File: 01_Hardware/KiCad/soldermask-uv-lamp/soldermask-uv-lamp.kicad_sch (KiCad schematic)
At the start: 12 parts, among them J1 USB_C_Receptacle_USB2.0_16P, Q1 BC817

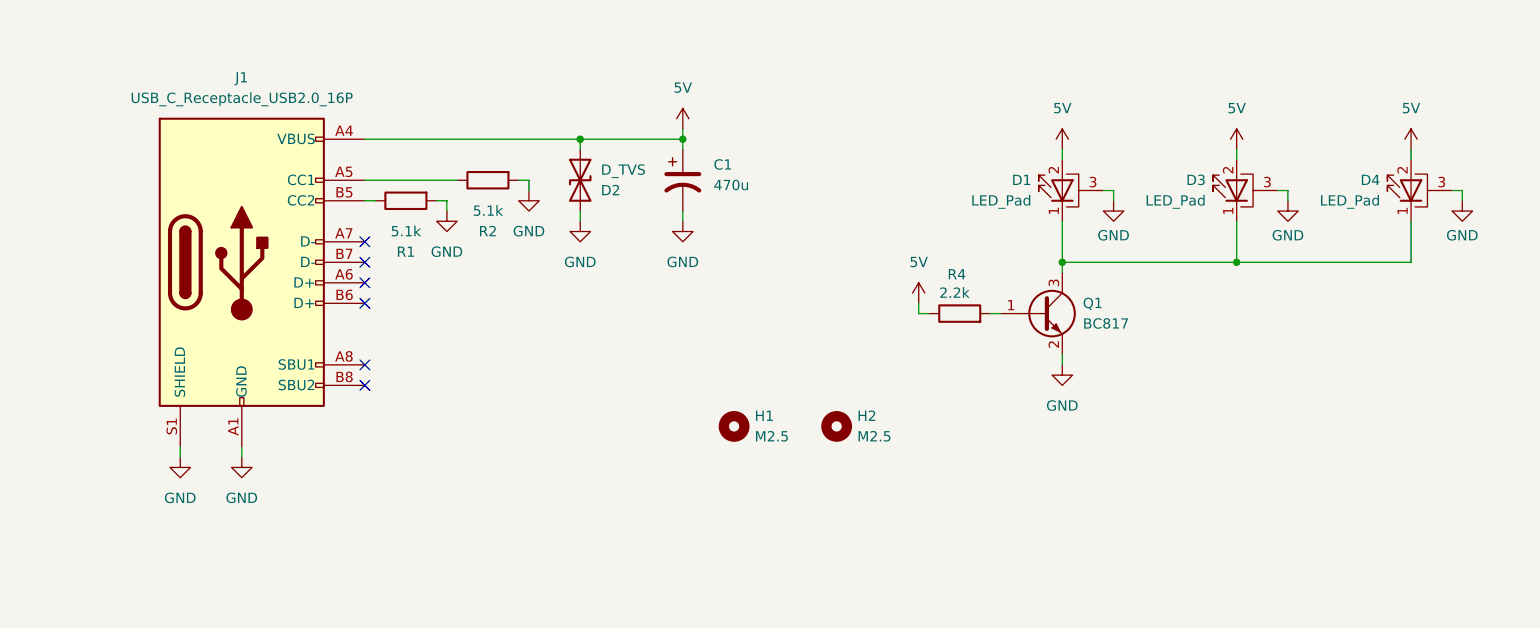
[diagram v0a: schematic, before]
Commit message: Added captions to schematics and pcb design
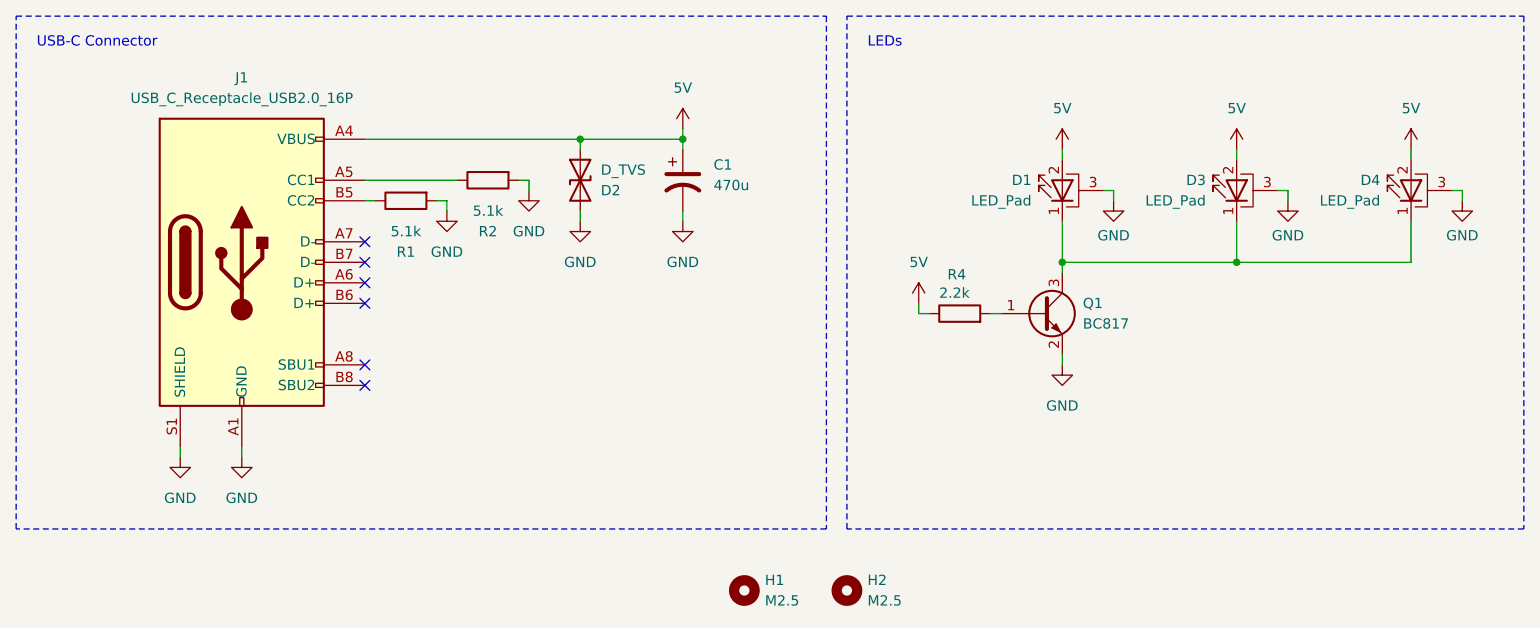
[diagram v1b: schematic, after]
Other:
- note added: "LEDs"
- note added: "USB-C Connector"
- company: (none) -> Szymon Wąchała
- title: (none) -> Soldermask UV Lamp
- moved on the sheet: H1, H2
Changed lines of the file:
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@@
 	(generator_version "9.0")
 	(paper "A4")
+	(title_block
+		(title "Soldermask UV Lamp")
+		(date "2025-11-21")
+		(rev "0.1")
+		(company "Szymon Wąchała")
+	)
+	(rectangle
+		(start 153.67 63.5)
+		(end 237.49 127)
+		(stroke
+			(width 0)
+			(type dash_dot)
+		)
+		(fill
+			(type none)
+		)
+	)
+	(rectangle
+		(start 50.8 63.5)
+		(end 151.13 127)
+		(stroke
+			(width 0)
+			(type dash_dot)
+		)
+		(fill
+			(type none)
+		)
+	)
+	(text "USB-C Connector"
+		(exclude_from_sim no)
+		(at 53.34 66.802 0)
+		(effects
+			(font
+				(size 1.27 1.27)
+			)
+			(justify left)
+		)
+	)
+	(text "LEDs"
+		(exclude_from_sim no)
+		(at 156.21 66.802 0)
+		(effects
+			(font
+				(size 1.27 1.27)
+			)
+			(justify left)
+		)
+	)
 	(junction
 		(at 120.65 78.74)
@@
 	(symbol
 		(lib_id "Mechanical:MountingHole")
-		(at 152.4 114.3 0)
+		(at 153.67 134.62 0)
 		(unit 1)
 		(exclude_from_sim no)
@@
 		(fields_autoplaced yes)
 		(property "Reference" "H2"
-			(at 154.94 113.0299 0)
+			(at 156.21 133.3499 0)
 			(effects
 				(font
@@
 		)
 		(property "Value" "M2.5"
-			(at 154.94 115.5699 0)
+			(at 156.21 135.8899 0)
 			(effects
 				(font
@@
 		)
 		(property "Footprint" "MountingHole:MountingHole_2.7mm_M2.5"
-			(at 152.4 114.3 0)
+			(at 153.67 134.62 0)
 			(effects
 				(font
@@
 		)
 		(property "Datasheet" "~"
-			(at 152.4 114.3 0)
+			(at 153.67 134.62 0)
 			(effects
 				(font
@@
 		)
 		(property "Description" "Mounting Hole without connection"
-			(at 152.4 114.3 0)
+			(at 153.67 134.62 0)
 			(effects
 				(font
@@
 	(symbol
 		(lib_id "Mechanical:MountingHole")
-		(at 139.7 114.3 0)
+		(at 140.97 134.62 0)
 		(unit 1)
 		(exclude_from_sim no)
@@
 		(fields_autoplaced yes)
 		(property "Reference" "H1"
-			(at 142.24 113.0299 0)
+			(at 143.51 133.3499 0)
 			(effects
 				(font
@@
 		)
 		(property "Value" "M2.5"
-			(at 142.24 115.5699 0)
+			(at 143.51 135.8899 0)
 			(effects
 				(font
@@
 		)
 		(property "Footprint" "MountingHole:MountingHole_2.7mm_M2.5"
-			(at 139.7 114.3 0)
+			(at 140.97 134.62 0)
 			(effects
 				(font
@@
 		)
 		(property "Datasheet" "~"
-			(at 139.7 114.3 0)
+			(at 140.97 134.62 0)
 			(effects
 				(font
@@
 		)
 		(property "Description" "Mounting Hole without connection"
-			(at 139.7 114.3 0)
-			(effects
-				(font
+			(at 140.97 134.62 0)
+			(effects
+				(font
